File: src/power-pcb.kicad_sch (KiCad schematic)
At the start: 6 parts, among them J1 PWR Supply Port, J2 Arduino Terminal, J3 Motor 2 Terminal, J4 Motor 1 Terminal, U1 L2596S, U2 Mini PWM Controller

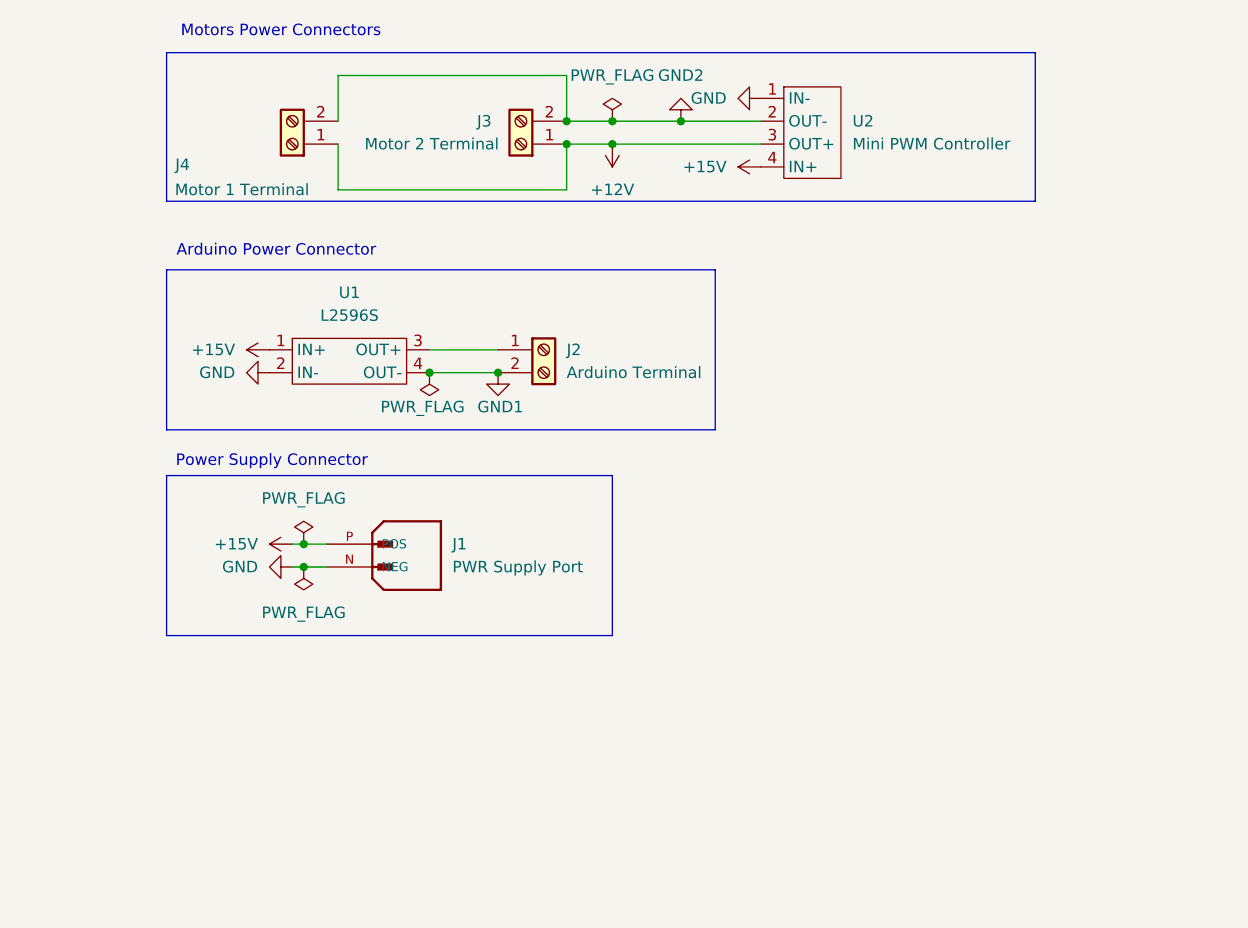
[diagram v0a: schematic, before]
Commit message: Arduino and motors
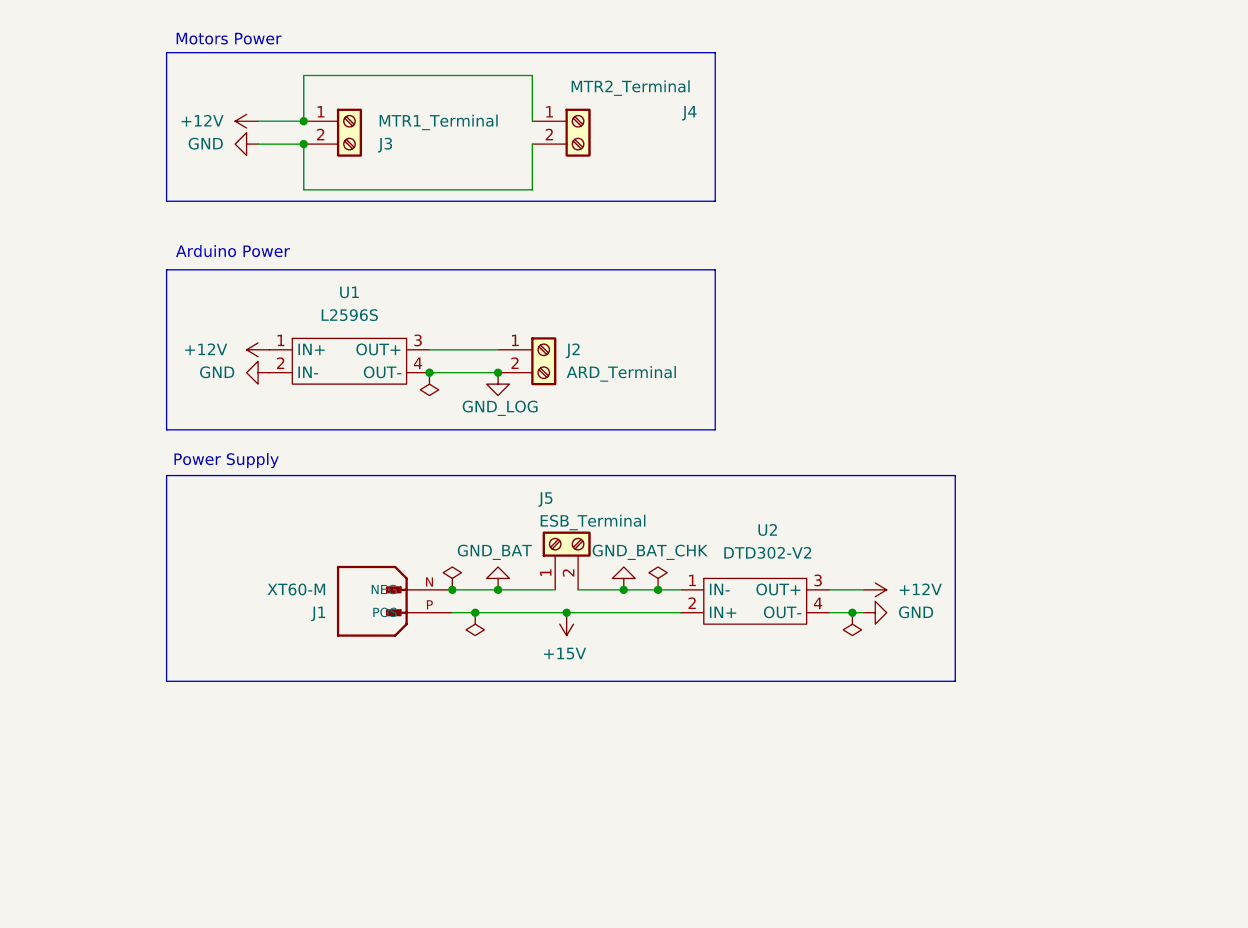
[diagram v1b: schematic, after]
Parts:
- removed U2: Mini PWM Controller, Converters_DCDC_Custom:Mini_PWM_Controller, symbol DCDC_Converters_Custom:Mini_PWM_Controller
- added J5: ESB_Terminal, Connector_Phoenix_GMSTB:PhoenixContact_GMSTBA_2,5_2-G-7,62_1x02_P7.62mm_Horizontal, symbol Connector:Screw_Terminal_01x02
- added U2: DTD302-V2, Converters_DCDC_Custom:DTD302-V2, symbol DCDC_Converters_Custom:DTD302-V2
- J1: value PWR Supply Port -> XT60-M
- J2: value Arduino Terminal -> ARD_Terminal; footprint TerminalBlock:TerminalBlock_Altech_AK300-2_P5.00mm -> Connector_Phoenix_GMSTB:PhoenixContact_GMSTBA_2,5_2-G-7,62_1x02_P7.62mm_Horizontal
- J3: value Motor 2 Terminal -> MTR1_Terminal; footprint TerminalBlock:TerminalBlock_Altech_AK300-2_P5.00mm -> Connector_Phoenix_GMSTB:PhoenixContact_GMSTBA_2,5_2-G-7,62_1x02_P7.62mm_Horizontal
- J4: value Motor 1 Terminal -> MTR2_Terminal; footprint TerminalBlock:TerminalBlock_Altech_AK300-2_P5.00mm -> Connector_Phoenix_GMSTB:PhoenixContact_GMSTBA_2,5_2-G-7,62_1x02_P7.62mm_Horizontal
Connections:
- net GND2 is gone; now on net GND: J3.2 (Pin_2), J4.2 (Pin_2)
- net +12V: now also U1.1 (IN+), U2.3 (OUT+)
- net +15V: now also U2.2 (IN+); no longer U1.1 (IN+)
- net GND: now also U2.4 (OUT-); no longer J1.N (NEG)
- net GND1 renamed GND_LOG
- new net GND_BAT: J1.N (NEG), J5.1 (Pin_1)
- new net GND_BAT_CHK: J5.2 (Pin_2), U2.1 (IN-)
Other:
- note added: "Arduino Power"
- note added: "Motors Power"
- note added: "Power Supply"
- note removed: "Arduino Power Connector"
- note removed: "Motors Power Connectors"
- note removed: "Power Supply Connector"
- company: (none) -> Hexobot SLSC
- title: (none) -> Power PCB
- moved on the sheet: J1, J3, J4

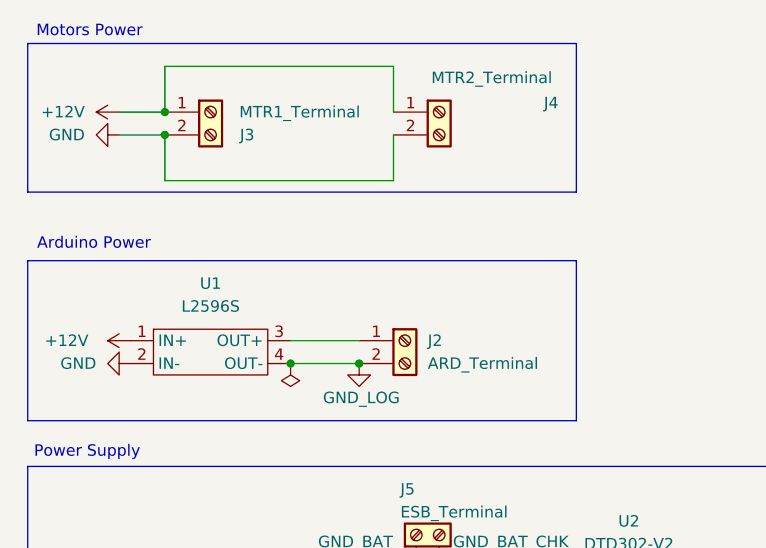
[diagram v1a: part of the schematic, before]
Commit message: Fix connections order on pwoer connectors
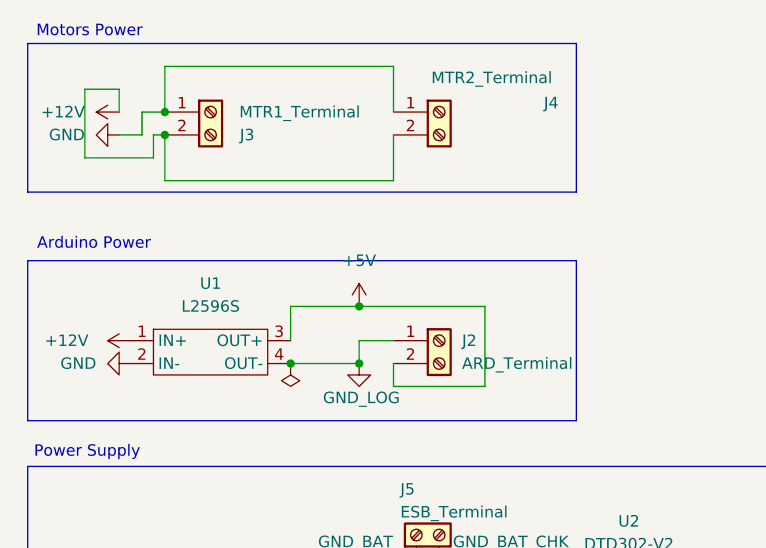
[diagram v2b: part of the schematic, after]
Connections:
- net +12V: now also J3.2 (Pin_2), J4.2 (Pin_2); no longer J3.1 (Pin_1), J4.1 (Pin_1)
- net GND: now also J3.1 (Pin_1), J4.1 (Pin_1); no longer J3.2 (Pin_2), J4.2 (Pin_2)
- net GND_LOG: now also J2.1 (Pin_1); no longer J2.2 (Pin_2)
- net +5V: now reaches U1.3 (OUT+)
- net +5V: now also J2.2 (Pin_2); no longer J2.1 (Pin_1)
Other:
- moved on the sheet: J2
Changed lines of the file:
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@@
+	)
+	(junction
+		(at 179.07 67.31)
+		(diameter 0)
+		(color 0 0 0 0)
+	)
+	(junction
+		(at 218.44 119.38)
+		(diameter 0)
+		(color 0 0 0 0)
 	)
 	(junction
@@
 	)
 	(junction
-		(at 179.07 67.31)
+		(at 214.63 119.38)
+		(diameter 0)
+		(color 0 0 0 0)
+	)
+	(junction
+		(at 193.04 95.25)
+		(diameter 0)
+		(color 0 0 0 0)
+	)
+	(junction
+		(at 200.66 119.38)
+		(diameter 0)
+		(color 0 0 0 0)
+	)
+	(junction
+		(at 240.03 121.92)
+		(diameter 0)
+		(color 0 0 0 0)
+	)
+	(junction
+		(at 200.66 88.9)
+		(diameter 0)
+		(color 0 0 0 0)
+	)
+	(junction
+		(at 198.12 121.92)
+		(diameter 0)
+		(color 0 0 0 0)
+	)
+	(junction
+		(at 195.58 119.38)
 		(diameter 0)
 		(color 0 0 0 0)
@@
 	)
 	(junction
-		(at 218.44 119.38)
-		(diameter 0)
-		(color 0 0 0 0)
-	)
-	(junction
-		(at 214.63 119.38)
-		(diameter 0)
-		(color 0 0 0 0)
-	)
-	(junction
-		(at 193.04 95.25)
-		(diameter 0)
-		(color 0 0 0 0)
-	)
-	(junction
-		(at 200.66 119.38)
-		(diameter 0)
-		(color 0 0 0 0)
-	)
-	(junction
-		(at 240.03 121.92)
-		(diameter 0)
-		(color 0 0 0 0)
-	)
-	(junction
-		(at 198.12 121.92)
-		(diameter 0)
-		(color 0 0 0 0)
-	)
-	(junction
-		(at 195.58 119.38)
-		(diameter 0)
-		(color 0 0 0 0)
-	)
-	(junction
 		(at 208.28 121.92)
 		(diameter 0)
@@
 	(wire
 		(pts
-			(xy 179.07 69.85) (xy 173.99 69.85)
+			(xy 177.8 72.39) (xy 177.8 69.85)
 		)
 		(stroke
@@
 	(wire
 		(pts
+			(xy 204.47 97.79) (xy 204.47 95.25)
+		)
+		(stroke
+			(width 0)
+			(type default)
+		)
+	)
+	(wire
+		(pts
 			(xy 198.12 121.92) (xy 208.28 121.92)
 		)
@@
 	(wire
 		(pts
+			(xy 173.99 64.77) (xy 170.18 64.77)
+		)
+		(stroke
+			(width 0)
+			(type default)
+		)
+	)
+	(wire
+		(pts
+			(xy 193.04 88.9) (xy 200.66 88.9)
+		)
+		(stroke
+			(width 0)
+			(type default)
+		)
+	)
+	(wire
+		(pts
+			(xy 204.47 92.71) (xy 200.66 92.71)
+		)
+		(stroke
+			(width 0)
+			(type default)
+		)
+	)
+	(wire
+		(pts
 			(xy 204.47 62.23) (xy 204.47 67.31)
 		)
@@
 	(wire
 		(pts
-			(xy 193.04 92.71) (xy 200.66 92.71)
+			(xy 177.8 69.85) (xy 179.07 69.85)
 		)
 		(stroke
@@
 	(wire
 		(pts
-			(xy 179.07 67.31) (xy 173.99 67.31)
+			(xy 176.53 69.85) (xy 176.53 67.31)
+		)
+		(stroke
+			(width 0)
+			(type default)
+		)
+	)
+	(wire
+		(pts
+			(xy 200.66 88.9) (xy 214.63 88.9)
+		)
+		(stroke
+			(width 0)
+			(type default)
+		)
+	)
+	(wire
+		(pts
+			(xy 173.99 69.85) (xy 176.53 69.85)
 		)
 		(stroke
@@
 	(wire
 		(pts
+			(xy 170.18 64.77) (xy 170.18 72.39)
+		)
+		(stroke
+			(width 0)
+			(type default)
+		)
+	)
+	(wire
+		(pts
 			(xy 193.04 95.25) (xy 200.66 95.25)
 		)
@@
 	(wire
 		(pts
+			(xy 176.53 67.31) (xy 179.07 67.31)
+		)
+		(stroke
+			(width 0)
+			(type default)
+		)
+	)
+	(wire
+		(pts
+			(xy 193.04 92.71) (xy 193.04 88.9)
+		)
+		(stroke
+			(width 0)
+			(type default)
+		)
+	)
+	(wire
+		(pts
+			(xy 173.99 67.31) (xy 173.99 64.77)
+		)
+		(stroke
+			(width 0)
+			(type default)
+		)
+	)
+	(wire
+		(pts
 			(xy 179.07 69.85) (xy 179.07 74.93)
 		)
@@
 	(wire
 		(pts
+			(xy 200.66 92.71) (xy 200.66 95.25)
+		)
+		(stroke
+			(width 0)
+			(type default)
+		)
+	)
+	(wire
+		(pts
+			(xy 214.63 97.79) (xy 204.47 97.79)
+		)
+		(stroke
+			(width 0)
+			(type default)
+		)
+	)
+	(wire
+		(pts
 			(xy 209.55 119.38) (xy 214.63 119.38)
+		)
+		(stroke
+			(width 0)
+			(type default)
+		)
+	)
+	(wire
+		(pts
+			(xy 214.63 88.9) (xy 214.63 97.79)
+		)
+		(stroke
+			(width 0)
+			(type default)
+		)
+	)
+	(wire
+		(pts
+			(xy 170.18 72.39) (xy 177.8 72.39)
 		)
 		(stroke
@@
 	(symbol
 		(lib_id "Connector:Screw_Terminal_01x02")
-		(at 205.74 92.71 0)
+		(at 209.55 92.71 0)
 		(unit 1)
 		(exclude_from_sim no)
@@
 		(fields_autoplaced yes)
 		(property "Reference" "J2"
-			(at 208.28 92.7099 0)
+			(at 212.09 92.7099 0)
 			(effects
 				(font
@@
 		)
 		(property "Value" "ARD_Terminal"
-			(at 208.28 95.2499 0)
+			(at 212.09 95.2499 0)
 			(effects
 				(font
@@
 		)
 		(property "Footprint" "Connector_Phoenix_GMSTB:PhoenixContact_GMSTBA_2,5_2-G-7,62_1x02_P7.62mm_Horizontal"
-			(at 205.74 92.71 0)
+			(at 209.55 92.71 0)
 			(effects
 				(font
@@
 		)
 		(property "Datasheet" "~"
-			(at 205.74 92.71 0)
+			(at 209.55 92.71 0)
 			(effects
 				(font
@@
 		)
 		(property "Description" "Generic screw terminal, single row, 01x02, script generated (kicad-library-utils/schlib/autogen/connector/)"
-			(at 205.74 92.71 0)
+			(at 209.55 92.71 0)
 			(effects
 				(font
@@
 					(unit 1)
 				)
+			)
+		)
+	)
+	(symbol
+		(lib_id "power:+5V")
+		(at 200.66 88.9 0)
+		(unit 1)
+		(exclude_from_sim no)
+		(in_bom yes)
+		(on_board yes)
+		(dnp no)
+		(fields_autoplaced yes)
+		(property "Reference" "#PWR09"
+			(at 200.66 92.71 0)
+			(effects
+				(font
+					(size 1.27 1.27)
+				)
+				(hide yes)
+			)
+		)
+		(property "Value" "+5V"
+			(at 200.66 83.82 0)
+			(effects
+				(font
+					(size 1.27 1.27)
+				)
+			)
+		)
+		(property "Footprint" ""
+			(at 200.66 88.9 0)
+			(effects
+				(font
+					(size 1.27 1.27)
+				)
+				(hide yes)
+			)
+		)
+		(property "Datasheet" ""
+			(at 200.66 88.9 0)
+			(effects
+				(font
+					(size 1.27 1.27)
+				)
+				(hide yes)
+			)
+		)
+		(property "Description" "Power symbol creates a global label with name \"+5V\""
+			(at 200.66 88.9 0)
+			(effects
+				(font
+					(size 1.27 1.27)
+				)
+				(hide yes)
+			)
+		)
+		(pin "1"
+		)
+		(instances
+			(project "power-pcb"
+				(path "/f227e403-efea-4f37-b23c-677f2ad96ae4"
+					(reference "#PWR09")
+					(unit 1)
+				)

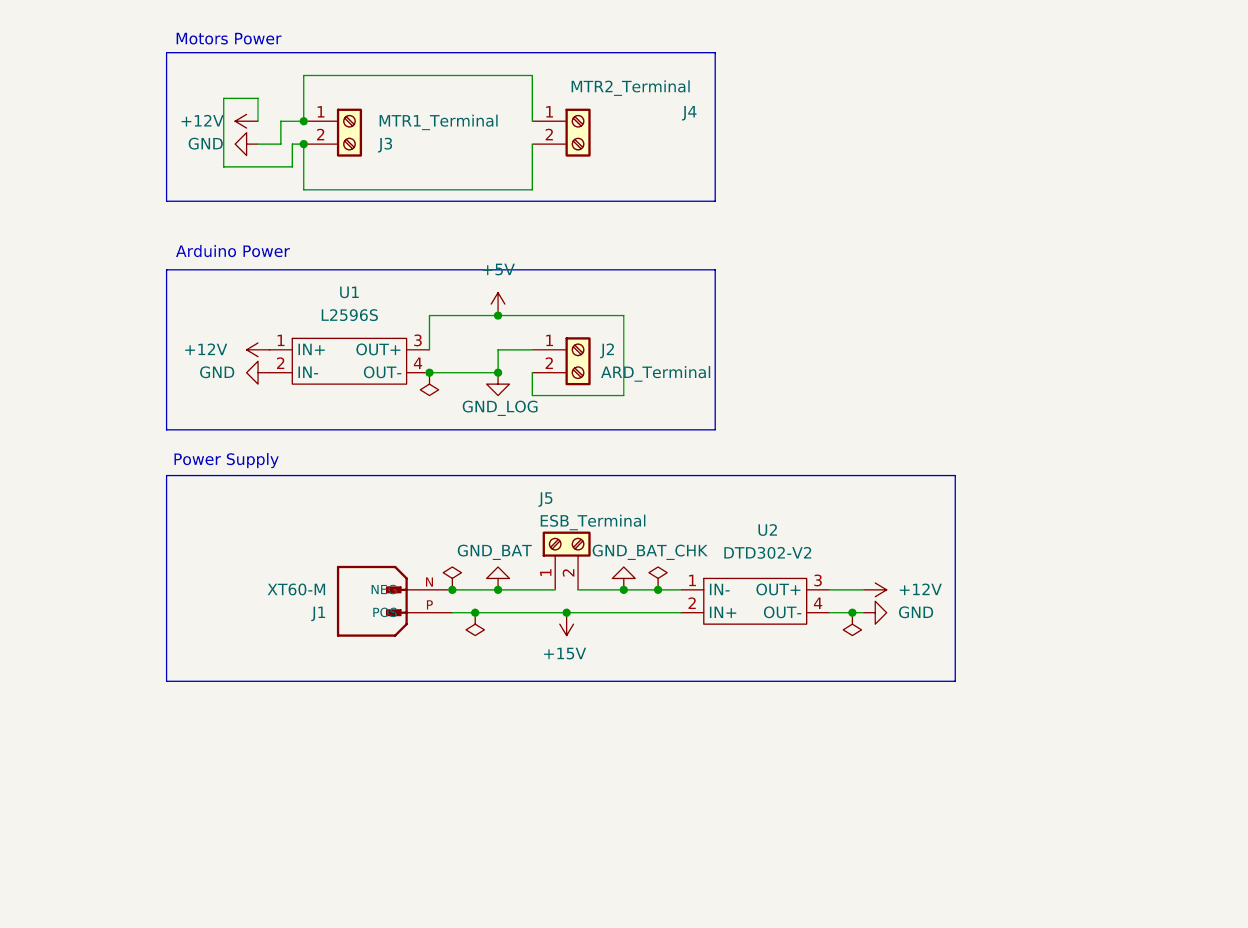
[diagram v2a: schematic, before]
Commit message: Add relay
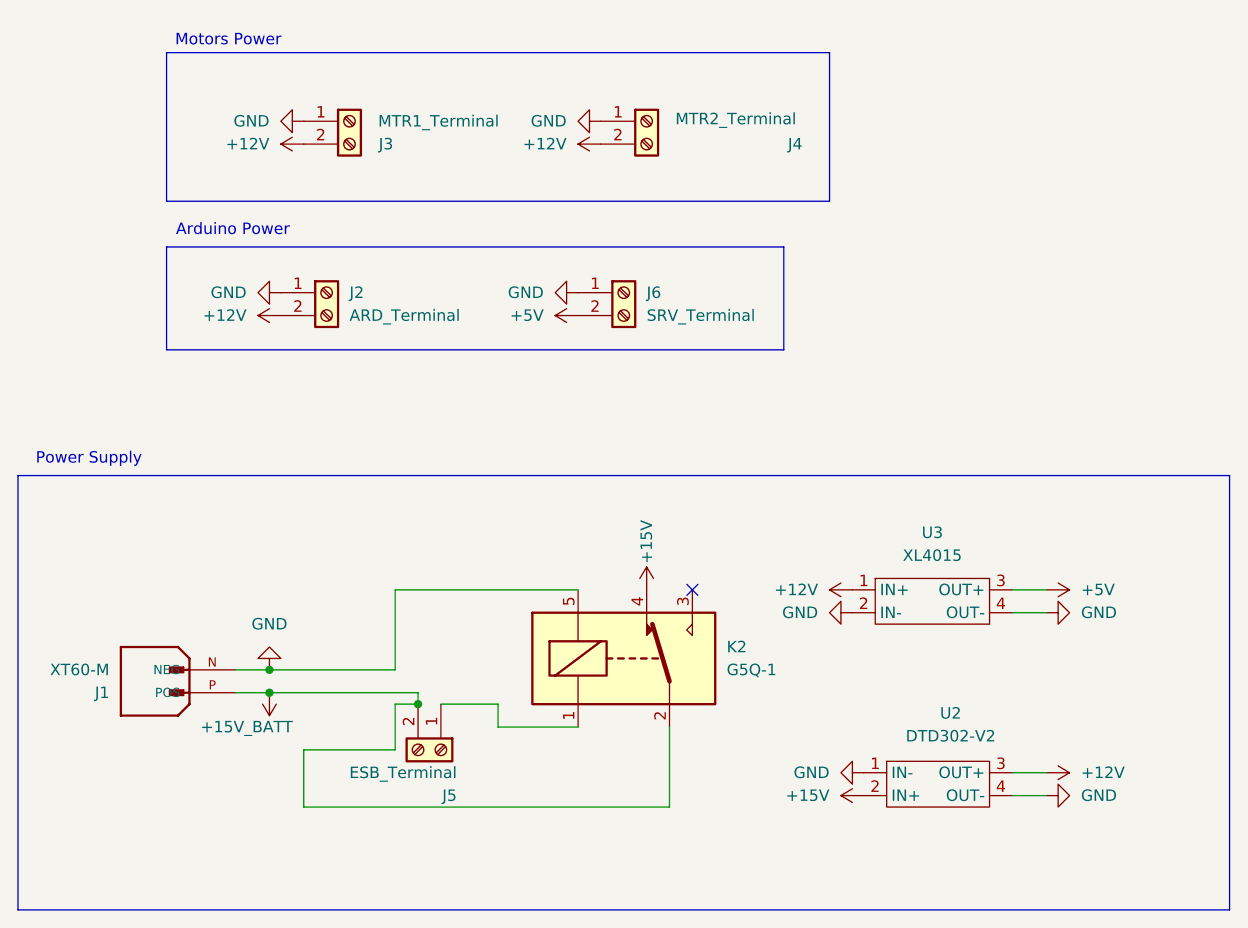
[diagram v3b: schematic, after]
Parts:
- removed U1: L2596S, Converters_DCDC_Custom:L2596S, symbol DCDC_Converters_Custom:L2596S
- added J6: SRV_Terminal, Connector_Phoenix_GMSTB:PhoenixContact_GMSTBA_2,5_2-G-7,62_1x02_P7.62mm_Horizontal, symbol Connector:Screw_Terminal_01x02
- added K2: G5Q-1, Relay_THT:Relay_SPDT_Omron-G5Q-1, symbol Relay:G5Q-1
- added U3: XL4015, Converters_DCDC_Custom:L2596S, symbol DCDC_Converters_Custom:XL4015
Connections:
- net GND_LOG is gone; now on net GND: J2.1 (Pin_1)
- net +12V: now also J2.2 (Pin_2), U3.1 (IN+)
- net +15V: now also K2.4; no longer J1.P (POS)
- net +5V: now also J6.2 (Pin_2), U3.3 (OUT+); no longer J2.2 (Pin_2)
- net GND: now also J1.N (NEG), U2.1 (IN-), J6.1 (Pin_1), K2.5, U3.2 (IN-), U3.4 (OUT-)
- net GND_BAT: no longer names the net of J5.1 (Pin_1)
- net GND_BAT: now also K2.1; no longer J1.N (NEG)
- net GND_BAT_CHK renamed +15V_BATT
- net +15V_BATT: now also J1.P (POS), K2.2; no longer U2.1 (IN-)
- no-connect marks 0 -> 1
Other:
- moved on the sheet: J1, J2, J4, J5, U2
